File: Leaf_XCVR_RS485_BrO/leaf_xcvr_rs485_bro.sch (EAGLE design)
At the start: 11 parts, among them U1 RS485_XCVR_SN65HVD178X

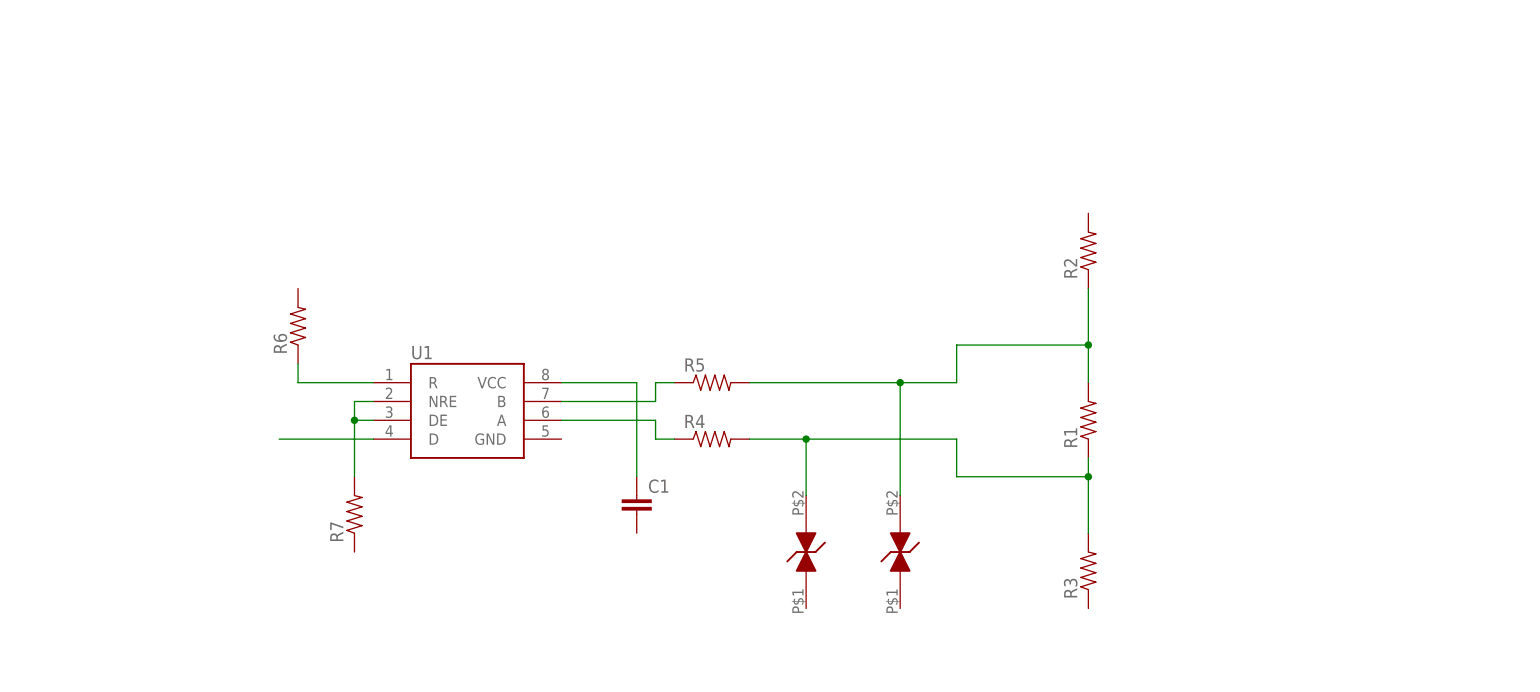
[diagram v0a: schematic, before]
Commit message: new xcvr board for mockups
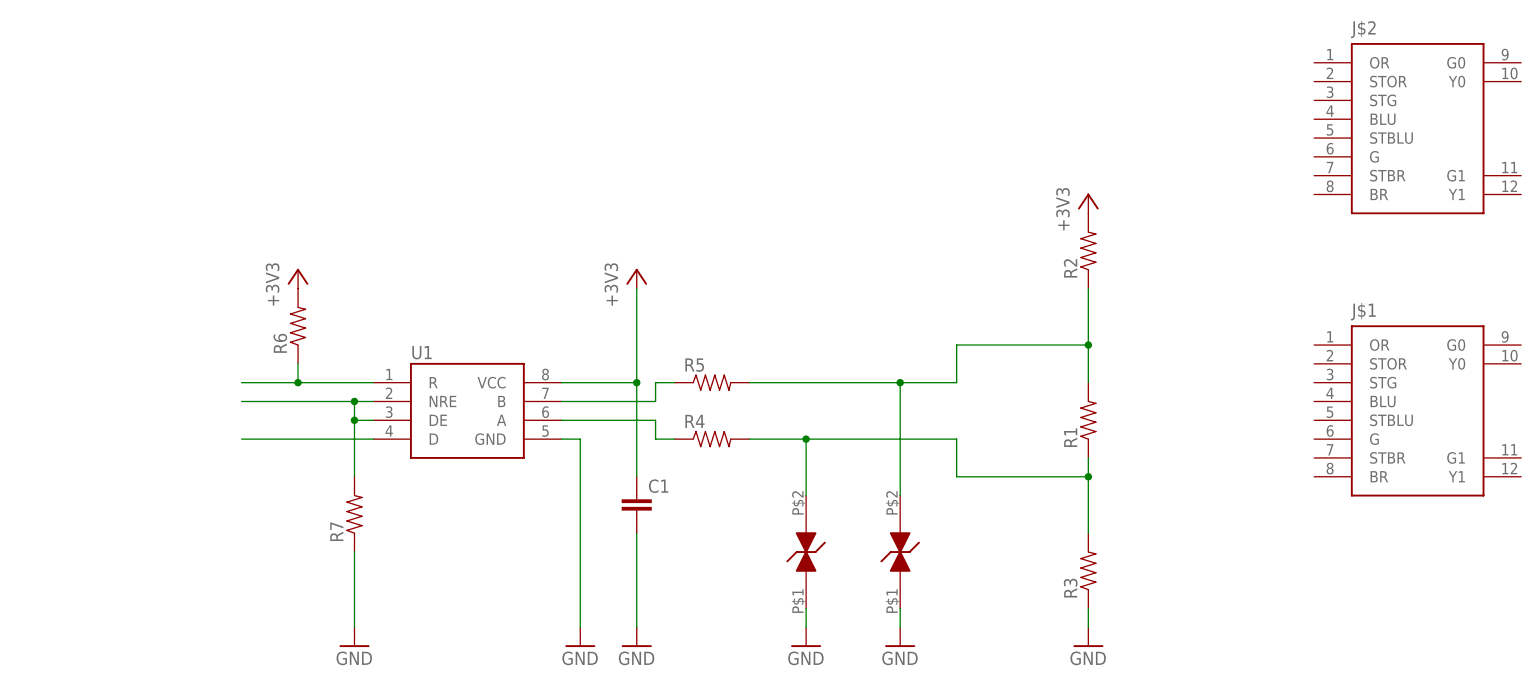
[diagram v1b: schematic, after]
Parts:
- added J$1, J$2: (no value), stepOSP:RJ45_RJHSE_508X
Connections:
- removed net N$3: C1.1, U1.VCC
- new net +3V3: C1.1, R2.2, R6.2, U1.VCC
- new net GND: C1.2, D1.P$1, D2.P$1, R3.1, R7.1, U1.GND
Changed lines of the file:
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@@
 <part name="R6" library="stepOSP" deviceset="0603_RES" device=""/>
 <part name="R7" library="stepOSP" deviceset="0603_RES" device=""/>
+<part name="+3V1" library="supply1" deviceset="+3V3" device=""/>
+<part name="+3V2" library="supply1" deviceset="+3V3" device=""/>
+<part name="+3V3" library="supply1" deviceset="+3V3" device=""/>
+<part name="GND1" library="supply1" deviceset="GND" device=""/>
+<part name="GND2" library="supply1" deviceset="GND" device=""/>
+<part name="GND3" library="supply1" deviceset="GND" device=""/>
+<part name="GND4" library="supply1" deviceset="GND" device=""/>
+<part name="GND5" library="supply1" deviceset="GND" device=""/>
+<part name="GND6" library="supply1" deviceset="GND" device=""/>
+<part name="J$1" library="stepOSP" deviceset="RJ45_RJHSE_508X" device=""/>
+<part name="J$2" library="stepOSP" deviceset="RJ45_RJHSE_508X" device=""/>
 </parts>
 <sheets>
@@
 <instance part="R6" gate="G$1" x="38.1" y="58.42" rot="R90"/>
 <instance part="R7" gate="G$1" x="45.72" y="33.02" rot="R90"/>
+<instance part="+3V1" gate="G$1" x="38.1" y="66.04"/>
+<instance part="+3V2" gate="G$1" x="144.78" y="76.2"/>
+<instance part="+3V3" gate="G$1" x="83.82" y="66.04"/>
+<instance part="GND1" gate="1" x="83.82" y="15.24"/>
+<instance part="GND2" gate="1" x="119.38" y="15.24"/>
+<instance part="GND3" gate="1" x="106.68" y="15.24"/>
+<instance part="GND4" gate="1" x="144.78" y="15.24"/>
+<instance part="GND5" gate="1" x="45.72" y="15.24"/>
+<instance part="GND6" gate="1" x="76.2" y="15.24"/>
+<instance part="J$1" gate="G$1" x="185.42" y="45.72"/>
+<instance part="J$2" gate="G$1" x="185.42" y="83.82"/>
 </instances>
 <busses>
 </busses>
 <nets>
-<net name="N$3" class="0">
-<segment>
-<pinref part="U1" gate="G$1" pin="VCC"/>
-<pinref part="C1" gate="G$1" pin="1"/>
-<wire x1="73.66" y1="50.8" x2="83.82" y2="50.8" width="0.1524" layer="91"/>
-<wire x1="83.82" y1="50.8" x2="83.82" y2="38.1" width="0.1524" layer="91"/>
-</segment>
-</net>
 <net name="N$1" class="0">
 <segment>
@@
 <wire x1="48.26" y1="45.72" x2="45.72" y2="45.72" width="0.1524" layer="91"/>
 <junction x="45.72" y="45.72"/>
+<wire x1="45.72" y1="48.26" x2="30.48" y2="48.26" width="0.1524" layer="91"/>
+<junction x="45.72" y="48.26"/>
 </segment>
 </net>
@@
 <wire x1="48.26" y1="50.8" x2="38.1" y2="50.8" width="0.1524" layer="91"/>
 <wire x1="38.1" y1="50.8" x2="38.1" y2="53.34" width="0.1524" layer="91"/>
+<wire x1="38.1" y1="50.8" x2="30.48" y2="50.8" width="0.1524" layer="91"/>
+<junction x="38.1" y="50.8"/>
 </segment>
 </net>
@@
 <segment>
 <pinref part="U1" gate="G$1" pin="D"/>
-<wire x1="48.26" y1="43.18" x2="35.56" y2="43.18" width="0.1524" layer="91"/>
+<wire x1="48.26" y1="43.18" x2="30.48" y2="43.18" width="0.1524" layer="91"/>
 </segment>
 </net>
+<net name="+3V3" class="0">
+<segment>
+<pinref part="R6" gate="G$1" pin="2"/>
+<pinref part="+3V1" gate="G$1" pin="+3V3"/>
+</segment>
+<segment>
+<pinref part="R2" gate="G$1" pin="2"/>
+<pinref part="+3V2" gate="G$1" pin="+3V3"/>
+</segment>
+<segment>
+<pinref part="U1" gate="G$1" pin="VCC"/>
+<pinref part="C1" gate="G$1" pin="1"/>
+<wire x1="73.66" y1="50.8" x2="83.82" y2="50.8" width="0.1524" layer="91"/>
+<wire x1="83.82" y1="50.8" x2="83.82" y2="38.1" width="0.1524" layer="91"/>
+<pinref part="+3V3" gate="G$1" pin="+3V3"/>
+<wire x1="83.82" y1="63.5" x2="83.82" y2="50.8" width="0.1524" layer="91"/>
+<junction x="83.82" y="50.8"/>
+</segment>
+</net>
+<net name="GND" class="0">
+<segment>
+<pinref part="C1" gate="G$1" pin="2"/>
+<pinref part="GND1" gate="1" pin="GND"/>
+<wire x1="83.82" y1="17.78" x2="83.82" y2="30.48" width="0.1524" layer="91"/>
+</segment>
+<segment>
+<pinref part="D2" gate="G$1" pin="P$1"/>
+<pinref part="GND2" gate="1" pin="GND"/>
+<wire x1="119.38" y1="17.78" x2="119.38" y2="20.32" width="0.1524" layer="91"/>
+</segment>
+<segment>
+<pinref part="D1" gate="G$1" pin="P$1"/>
+<pinref part="GND3" gate="1" pin="GND"/>
+<wire x1="106.68" y1="17.78" x2="106.68" y2="20.32" width="0.1524" layer="91"/>
+</segment>
+<segment>
+<pinref part="R3" gate="G$1" pin="1"/>
+<pinref part="GND4" gate="1" pin="GND"/>
+<wire x1="144.78" y1="17.78" x2="144.78" y2="20.32" width="0.1524" layer="91"/>
+</segment>
+<segment>
+<pinref part="R7" gate="G$1" pin="1"/>
+<pinref part="GND5" gate="1" pin="GND"/>
+<wire x1="45.72" y1="17.78" x2="45.72" y2="27.94" width="0.1524" layer="91"/>
+</segment>
+<segment>
+<pinref part="U1" gate="G$1" pin="GND"/>
+<wire x1="73.66" y1="43.18" x2="76.2" y2="43.18" width="0.1524" layer="91"/>
+<wire x1="76.2" y1="43.18" x2="76.2" y2="17.78" width="0.1524" layer="91"/>
+<pinref part="GND6" gate="1" pin="GND"/>
+</segment>
+</net>

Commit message: updating rs485 breakout
added a few new connectors and trying out some new designs
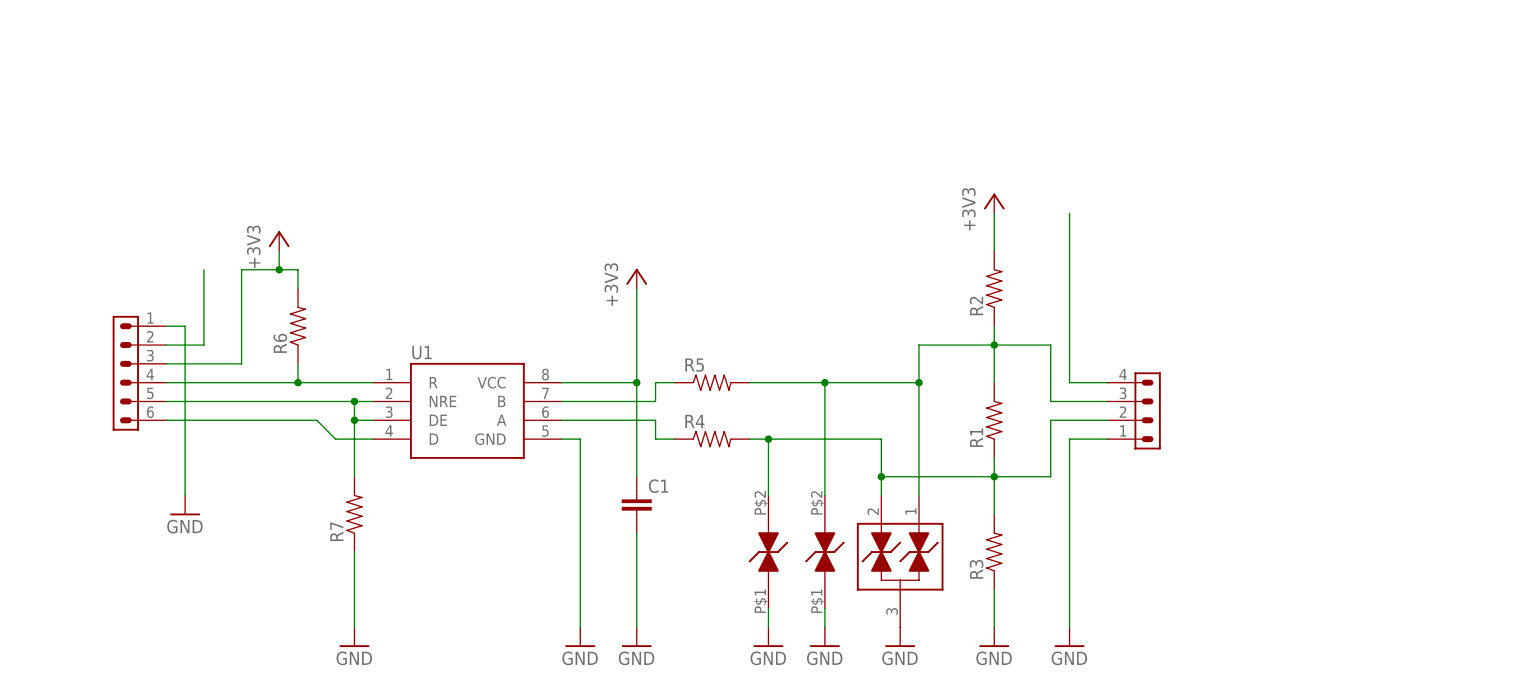
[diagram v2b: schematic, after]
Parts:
- removed J$1, J$2: (no value), stepOSP:RJ45_RJHSE_508X
- added D3: TVS_SOT-23, leaf:TVS_SOT-23
- added J1: CONN_6X1_JST_PA, leaf:CONN_6X1_JST_PA
- added J2: CONN_4X1_JST_PA, leaf:CONN_4X1_JST_PA
- C1: device stepOSP:0805_CAP -> stepOSP:0603_CAP
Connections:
- new net N$4: J1.2
- new net N$5: J2.4
- net +3V3: now also J1.3
- net GND: now also D3.3, J1.1, J2.1
- net N$10: now also J1.6
- net N$6: now also D3.2, J2.2
- net N$7: now also D3.1, J2.3
- net N$8: now also J1.5
- net N$9: now also J1.4
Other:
- moved on the sheet: R1, R2, R3

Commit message: latest and greatest
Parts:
- J1: value CONN_6X1_JST_PA -> CONN_7X1_JST_PA; device leaf:CONN_6X1_JST_PA -> leaf:CONN_7X1_JST_PA
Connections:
- removed net GND: C1.2, D1.P$1, D2.P$1, D3.3, J1.1, J2.1, R3.1, R7.1, U1.GND
- removed net N$4: J1.2
- removed net N$5: J2.4
- new net GND1: C1.2, D1.P$1, D2.P$1, D3.3, J1.3, R3.1, R7.1, U1.GND
- new net GND2: J1.1, J2.1
- new net V+: J1.2, J2.4
- net +3V3: now also J1.4; no longer J1.3
- net N$10: now also J1.7; no longer J1.6
- net N$8: now also J1.6; no longer J1.5
- net N$9: now also J1.5; no longer J1.4

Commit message: submission to OSHpark
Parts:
- added TP1, TP2, TP3, TP4, TP5, TP6, TP7, TP8, TP9: TP1, leaf:TP1
- added U$1: STEPS_LOGO, stepOSP:STEPS_LOGO
- C1: value (none) -> 0.1u
- R1: value (none) -> 120
- R4, R5: value (none) -> 10
- R6, R7: value (none) -> 3.3k
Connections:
- net +3V3: now also J1.5, TP6.P$1; no longer J1.4
- net GND1: now also D1.1, D2.1, J1.1, TP9.P$1; no longer D1.P$1, D2.P$1, J1.3
- net GND2: now also J1.7, TP8.P$1; no longer J1.1
- net N$10: now also J1.2, TP3.P$1; no longer J1.7
- net N$6: now also D1.2, TP2.P$1; no longer D1.P$2
- net N$7: now also D2.2, TP1.P$1; no longer D2.P$2
- net N$8: now also J1.3, TP5.P$1; no longer J1.6
- net N$9: now also J1.4, TP4.P$1; no longer J1.5
- net V+: now also J1.6, TP7.P$1; no longer J1.2
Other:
- moved on the sheet: R6
